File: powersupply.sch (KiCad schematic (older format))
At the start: 12 parts

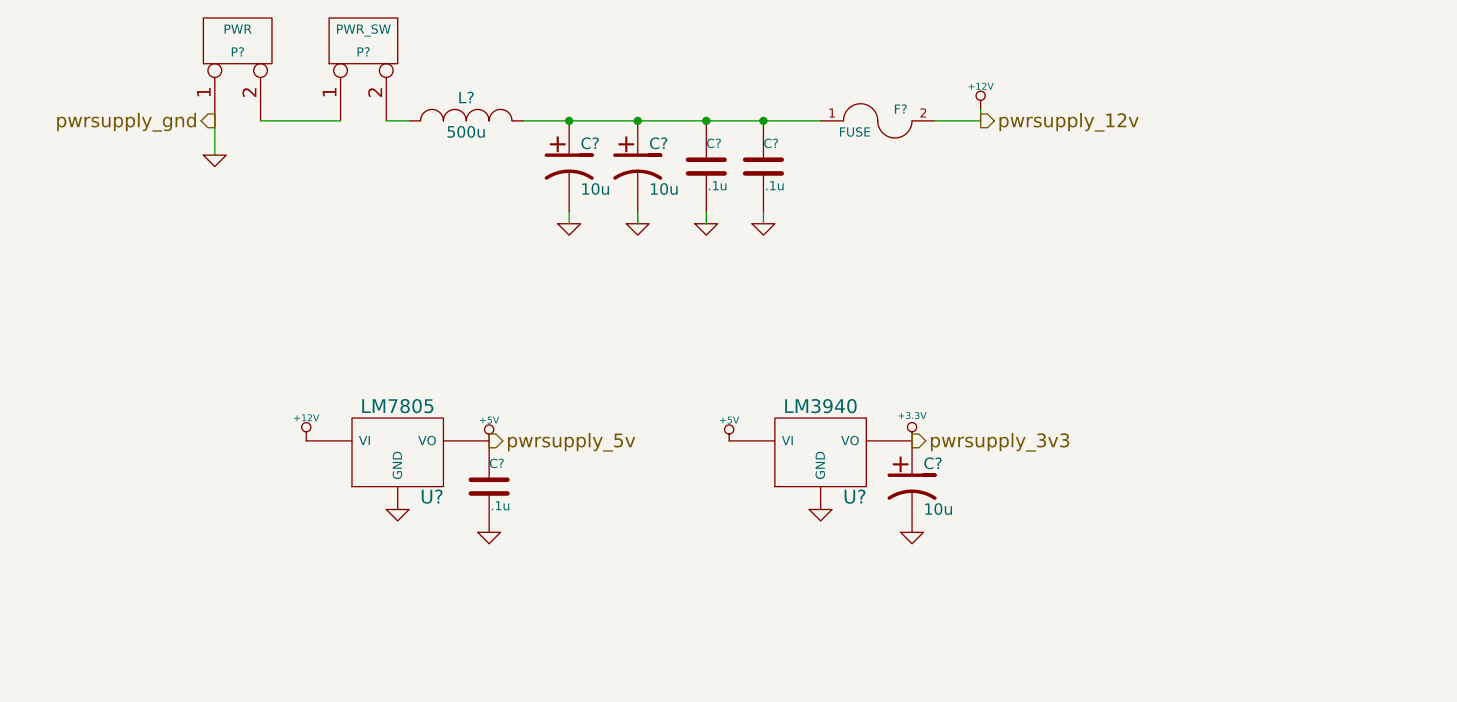
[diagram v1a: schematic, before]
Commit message: Annotated all schematics
- Added more caps to power supply
- Decided on power supply fuse part
- Changed 1n5711 SWR caps to BAT62
- Decided on MMBF170 for amp bias switch
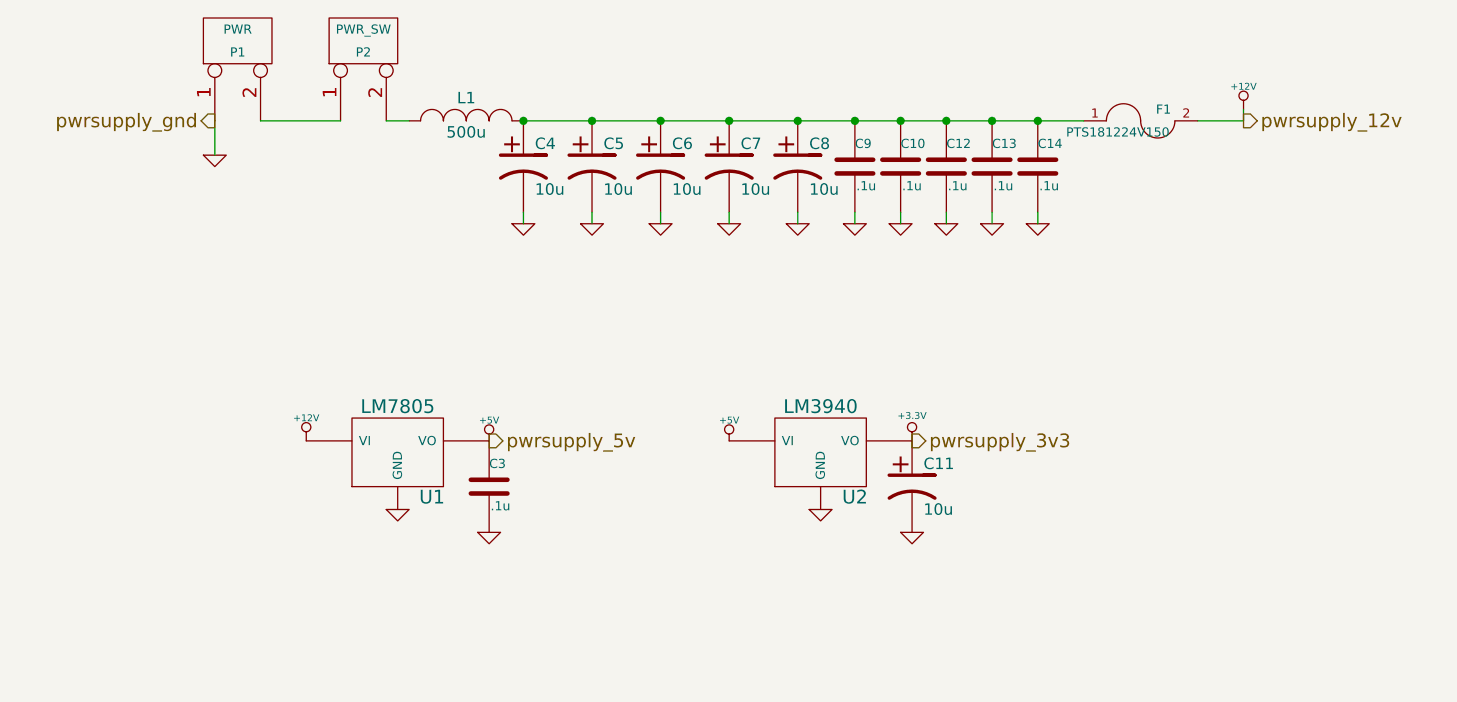
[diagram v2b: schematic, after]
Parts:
- removed C? (x2): .1u, symbol C
- added C10, C12, C13, C14, C9: .1u, symbol C
- added C6, C7, C8: 10u, symbol CP1
- F1: renamed from F?; value FUSE -> PTS181224V150
- gave numbers to parts that had none: 9
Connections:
- net GND: now also C10.2, C12.2, C13.2, C14.2, C6.2, C7.2, C8.2, C9.2
- net at C4.1, C5.1, F1.1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: now also C10.1, C12.1, C13.1, C14.1, C6.1, C7.1, C8.1, C9.1
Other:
- moved on the sheet: C4, C5, F1

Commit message: Associate more footprints
- Removed flyback diodes from amp
- Changed BAT62 -> SD101 (BAT62 is EOL)
- Changed R and C footprints for hand-soldered versions
- Associated through-hole cap footprints
- Associated regulator footprints
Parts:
- C10, C12, C13, C14, C3, C9: footprint (none) -> Capacitors_SMD:C_0805_HandSoldering
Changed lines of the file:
@@
 LIBS:transformers
 LIBS:qrpamp-cache
-EELAYER 24 0
+EELAYER 25 0
 EELAYER END
 $Descr A4 11693 8268
@@
 F 0 "P1" V 3150 2200 40  0000 C CNN
 F 1 "PWR" V 3250 2200 40  0000 C CNN
-F 2 "" H 3200 2200 60  0000 C CNN
+F 2 "" H 3200 2200 60  0001 C CNN
 F 3 "" H 3200 2200 60  0000 C CNN
 	1    3200 2200
@@
 F 0 "P2" V 3700 2200 40  0000 C CNN
 F 1 "PWR_SW" V 3800 2200 40  0000 C CNN
-F 2 "" H 3750 2200 60  0000 C CNN
+F 2 "" H 3750 2200 60  0001 C CNN
 F 3 "" H 3750 2200 60  0000 C CNN
 	1    3750 2200
@@
 F 0 "L1" H 4200 2650 50  0000 C CNN
 F 1 "500u" H 4200 2500 50  0000 C CNN
-F 2 "" H 4200 2550 60  0000 C CNN
+F 2 "" H 4200 2550 60  0001 C CNN
 F 3 "" H 4200 2550 60  0000 C CNN
 	1    4200 2550
@@
 F 0 "C4" H 4500 2850 50  0000 L CNN
 F 1 "10u" H 4500 2650 50  0000 L CNN
-F 2 "" H 4450 2750 60  0000 C CNN
+F 2 "" H 4450 2750 60  0001 C CNN
 F 3 "" H 4450 2750 60  0000 C CNN
 	1    4450 2750
@@
 F 0 "C5" H 4800 2850 50  0000 L CNN
 F 1 "10u" H 4800 2650 50  0000 L CNN
-F 2 "" H 4750 2750 60  0000 C CNN
+F 2 "" H 4750 2750 60  0001 C CNN
 F 3 "" H 4750 2750 60  0000 C CNN
 	1    4750 2750
@@
 F 0 "U1" H 4050 3804 60  0000 C CNN
 F 1 "LM7805" H 3900 4200 60  0000 C CNN
-F 2 "" H 3900 4000 60  0000 C CNN
+F 2 "" H 3900 4000 60  0001 C CNN
 F 3 "" H 3900 4000 60  0000 C CNN
 	1    3900 4000
@@
 F 0 "U2" H 5900 3804 60  0000 C CNN
 F 1 "LM3940" H 5750 4200 60  0000 C CNN
-F 2 "" H 5750 4000 60  0000 C CNN
+F 2 "" H 5750 4000 60  0001 C CNN
 F 3 "" H 5750 4000 60  0000 C CNN
 	1    5750 4000
@@
 F 0 "F1" H 7250 2600 40  0000 C CNN
 F 1 "PTS181224V150" H 7050 2500 40  0000 C CNN
-F 2 "" H 7150 2550 60  0000 C CNN
+F 2 "" H 7150 2550 60  0001 C CNN
 F 3 "" H 7150 2550 60  0000 C CNN
 	1    7150 2550
@@
 F 0 "C3" H 4300 4250 40  0000 L CNN
 F 1 ".1u" H 4306 4065 40  0000 L CNN
-F 2 "" H 4338 4000 30  0000 C CNN
+F 2 "Capacitors_SMD:C_0805_HandSoldering" H 4338 4000 30  0001 C CNN
 F 3 "" H 4300 4150 60  0000 C CNN
 	1    4300 4150
@@
 F 0 "C11" H 6200 4250 50  0000 L CNN
 F 1 "10u" H 6200 4050 50  0000 L CNN
-F 2 "" H 6150 4150 60  0000 C CNN
+F 2 "" H 6150 4150 60  0001 C CNN
 F 3 "" H 6150 4150 60  0000 C CNN
 	1    6150 4150
@@
 F 0 "C6" H 5100 2850 50  0000 L CNN
 F 1 "10u" H 5100 2650 50  0000 L CNN
-F 2 "" H 5050 2750 60  0000 C CNN
+F 2 "" H 5050 2750 60  0001 C CNN
 F 3 "" H 5050 2750 60  0000 C CNN
 	1    5050 2750
@@
 F 0 "C7" H 5400 2850 50  0000 L CNN
 F 1 "10u" H 5400 2650 50  0000 L CNN
-F 2 "" H 5350 2750 60  0000 C CNN
+F 2 "" H 5350 2750 60  0001 C CNN
 F 3 "" H 5350 2750 60  0000 C CNN
 	1    5350 2750
@@
 F 0 "C8" H 5700 2850 50  0000 L CNN
 F 1 "10u" H 5700 2650 50  0000 L CNN
-F 2 "" H 5650 2750 60  0000 C CNN
+F 2 "" H 5650 2750 60  0001 C CNN
 F 3 "" H 5650 2750 60  0000 C CNN
 	1    5650 2750
@@
 F 0 "C9" H 5900 2850 40  0000 L CNN
 F 1 ".1u" H 5906 2665 40  0000 L CNN
-F 2 "" H 5938 2600 30  0000 C CNN
+F 2 "Capacitors_SMD:C_0805_HandSoldering" H 5938 2600 30  0001 C CNN
 F 3 "" H 5900 2750 60  0000 C CNN
 	1    5900 2750
@@
 F 0 "C10" H 6100 2850 40  0000 L CNN
 F 1 ".1u" H 6106 2665 40  0000 L CNN
-F 2 "" H 6138 2600 30  0000 C CNN
+F 2 "Capacitors_SMD:C_0805_HandSoldering" H 6138 2600 30  0001 C CNN
 F 3 "" H 6100 2750 60  0000 C CNN
 	1    6100 2750
@@
 F 0 "C12" H 6300 2850 40  0000 L CNN
 F 1 ".1u" H 6306 2665 40  0000 L CNN
-F 2 "" H 6338 2600 30  0000 C CNN
+F 2 "Capacitors_SMD:C_0805_HandSoldering" H 6338 2600 30  0001 C CNN
 F 3 "" H 6300 2750 60  0000 C CNN
 	1    6300 2750
@@
 F 0 "C13" H 6500 2850 40  0000 L CNN
 F 1 ".1u" H 6506 2665 40  0000 L CNN
-F 2 "" H 6538 2600 30  0000 C CNN
+F 2 "Capacitors_SMD:C_0805_HandSoldering" H 6538 2600 30  0001 C CNN
 F 3 "" H 6500 2750 60  0000 C CNN
 	1    6500 2750
@@
 F 0 "C14" H 6700 2850 40  0000 L CNN
 F 1 ".1u" H 6706 2665 40  0000 L CNN
-F 2 "" H 6738 2600 30  0000 C CNN
+F 2 "Capacitors_SMD:C_0805_HandSoldering" H 6738 2600 30  0001 C CNN
 F 3 "" H 6700 2750 60  0000 C CNN
 	1    6700 2750

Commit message: Finished band filters schematic
- Associated last of the capacitors with footprints
- Associated inductors
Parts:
- C11, C4, C5, C6, C7, C8: footprint (none) -> Capacitors_ThroughHole:Capacitor5x11RM2.5
- U1: footprint (none) -> SMD_Packages:DPAK-2
- U2: footprint (none) -> SMD_Packages:TO-263
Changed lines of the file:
@@
 	3300 2550 3650 2550
 $Comp
-L GND #PWR20
+L GND #PWR020
 U 1 1 5470C747
 P 3100 2700
-F 0 "#PWR20" H 3100 2700 30  0001 C CNN
+F 0 "#PWR020" H 3100 2700 30  0001 C CNN
 F 1 "GND" H 3100 2630 30  0001 C CNN
 F 2 "" H 3100 2700 60  0000 C CNN
@@
 F 0 "C4" H 4500 2850 50  0000 L CNN
 F 1 "10u" H 4500 2650 50  0000 L CNN
-F 2 "" H 4450 2750 60  0001 C CNN
+F 2 "Capacitors_ThroughHole:Capacitor5x11RM2.5" H 4450 2750 60  0001 C CNN
 F 3 "" H 4450 2750 60  0000 C CNN
 	1    4450 2750
@@
 F 0 "C5" H 4800 2850 50  0000 L CNN
 F 1 "10u" H 4800 2650 50  0000 L CNN
-F 2 "" H 4750 2750 60  0001 C CNN
+F 2 "Capacitors_ThroughHole:Capacitor5x11RM2.5" H 4750 2750 60  0001 C CNN
 F 3 "" H 4750 2750 60  0000 C CNN
 	1    4750 2750
@@
 $EndComp
 $Comp
-L GND #PWR25
+L GND #PWR021
 U 1 1 5470C830
 P 4450 3000
-F 0 "#PWR25" H 4450 3000 30  0001 C CNN
+F 0 "#PWR021" H 4450 3000 30  0001 C CNN
 F 1 "GND" H 4450 2930 30  0001 C CNN
 F 2 "" H 4450 3000 60  0000 C CNN
@@
 $EndComp
 $Comp
-L GND #PWR26
+L GND #PWR022
 U 1 1 5470C83B
 P 4750 3000
-F 0 "#PWR26" H 4750 3000 30  0001 C CNN
+F 0 "#PWR022" H 4750 3000 30  0001 C CNN
 F 1 "GND" H 4750 2930 30  0001 C CNN
 F 2 "" H 4750 3000 60  0000 C CNN
@@
 	4750 2950 4750 3000
 $Comp
-L +12V #PWR39
+L +12V #PWR023
 U 1 1 5470C933
 P 7600 2500
-F 0 "#PWR39" H 7600 2450 20  0001 C CNN
+F 0 "#PWR023" H 7600 2450 20  0001 C CNN
 F 1 "+12V" H 7600 2600 30  0000 C CNN
 F 2 "" H 7600 2500 60  0000 C CNN
@@
 F 0 "U1" H 4050 3804 60  0000 C CNN
 F 1 "LM7805" H 3900 4200 60  0000 C CNN
-F 2 "" H 3900 4000 60  0001 C CNN
+F 2 "SMD_Packages:DPAK-2" H 3900 4000 60  0001 C CNN
 F 3 "" H 3900 4000 60  0000 C CNN
 	1    3900 4000
@@
 F 0 "U2" H 5900 3804 60  0000 C CNN
 F 1 "LM3940" H 5750 4200 60  0000 C CNN
-F 2 "" H 5750 4000 60  0001 C CNN
+F 2 "SMD_Packages:TO-263" H 5750 4000 60  0001 C CNN
 F 3 "" H 5750 4000 60  0000 C CNN
 	1    5750 4000
@@
 	7600 2550 7600 2500
 $Comp
-L GND #PWR22
+L GND #PWR024
 U 1 1 5470CBF4
 P 3900 4250
-F 0 "#PWR22" H 3900 4250 30  0001 C CNN
+F 0 "#PWR024" H 3900 4250 30  0001 C CNN
 F 1 "GND" H 3900 4180 30  0001 C CNN
 F 2 "" H 3900 4250 60  0000 C CNN
@@
 $EndComp
 $Comp
-L GND #PWR31
+L GND #PWR025
 U 1 1 5470CBFF
 P 5750 4250
-F 0 "#PWR31" H 5750 4250 30  0001 C CNN
+F 0 "#PWR025" H 5750 4250 30  0001 C CNN
 F 1 "GND" H 5750 4180 30  0001 C CNN
 F 2 "" H 5750 4250 60  0000 C CNN
@@
 $EndComp
 $Comp
-L +12V #PWR21
+L +12V #PWR026
 U 1 1 5470CC17
 P 3500 3950
-F 0 "#PWR21" H 3500 3900 20  0001 C CNN
+F 0 "#PWR026" H 3500 3900 20  0001 C CNN
 F 1 "+12V" H 3500 4050 30  0000 C CNN
 F 2 "" H 3500 3950 60  0000 C CNN
@@
 $EndComp
 $Comp
-L +5V #PWR23
+L +5V #PWR027
 U 1 1 5470CC25
 P 4300 3950
-F 0 "#PWR23" H 4300 4040 20  0001 C CNN
+F 0 "#PWR027" H 4300 4040 20  0001 C CNN
 F 1 "+5V" H 4300 4040 30  0000 C CNN
 F 2 "" H 4300 3950 60  0000 C CNN
@@
 $EndComp
 $Comp
-L +5V #PWR29
+L +5V #PWR028
 U 1 1 5470CC37
 P 5350 3950
-F 0 "#PWR29" H 5350 4040 20  0001 C CNN
+F 0 "#PWR028" H 5350 4040 20  0001 C CNN
 F 1 "+5V" H 5350 4040 30  0000 C CNN
 F 2 "" H 5350 3950 60  0000 C CNN
@@
 $EndComp
 $Comp
-L +3.3V #PWR34
+L +3.3V #PWR029
 U 1 1 5470CC44
 P 6150 3950
-F 0 "#PWR34" H 6150 3910 30  0001 C CNN
+F 0 "#PWR029" H 6150 3910 30  0001 C CNN
 F 1 "+3.3V" H 6150 4060 30  0000 C CNN
 F 2 "" H 6150 3950 60  0000 C CNN
@@
 F 0 "C11" H 6200 4250 50  0000 L CNN
 F 1 "10u" H 6200 4050 50  0000 L CNN
-F 2 "" H 6150 4150 60  0001 C CNN
+F 2 "Capacitors_ThroughHole:Capacitor5x11RM2.5" H 6150 4150 60  0001 C CNN
 F 3 "" H 6150 4150 60  0000 C CNN
 	1    6150 4150
@@
 $EndComp
 $Comp
-L GND #PWR24
+L GND #PWR030
 U 1 1 5470CCF4
 P 4300 4350
-F 0 "#PWR24" H 4300 4350 30  0001 C CNN
+F 0 "#PWR030" H 4300 4350 30  0001 C CNN
 F 1 "GND" H 4300 4280 30  0001 C CNN
 F 2 "" H 4300 4350 60  0000 C CNN
@@
 $EndComp
 $Comp
-L GND #PWR35
+L GND #PWR031
 U 1 1 5470CCFF
 P 6150 4350
-F 0 "#PWR35" H 6150 4350 30  0001 C CNN
+F 0 "#PWR031" H 6150 4350 30  0001 C CNN
 F 1 "GND" H 6150 4280 30  0001 C CNN
 F 2 "" H 6150 4350 60  0000 C CNN
@@
 F 0 "C6" H 5100 2850 50  0000 L CNN
 F 1 "10u" H 5100 2650 50  0000 L CNN
-F 2 "" H 5050 2750 60  0001 C CNN
+F 2 "Capacitors_ThroughHole:Capacitor5x11RM2.5" H 5050 2750 60  0001 C CNN
 F 3 "" H 5050 2750 60  0000 C CNN
 	1    5050 2750
@@
 F 0 "C7" H 5400 2850 50  0000 L CNN
 F 1 "10u" H 5400 2650 50  0000 L CNN
-F 2 "" H 5350 2750 60  0001 C CNN
+F 2 "Capacitors_ThroughHole:Capacitor5x11RM2.5" H 5350 2750 60  0001 C CNN
 F 3 "" H 5350 2750 60  0000 C CNN
 	1    5350 2750
@@
 F 0 "C8" H 5700 2850 50  0000 L CNN
 F 1 "10u" H 5700 2650 50  0000 L CNN
-F 2 "" H 5650 2750 60  0001 C CNN
+F 2 "Capacitors_ThroughHole:Capacitor5x11RM2.5" H 5650 2750 60  0001 C CNN
 F 3 "" H 5650 2750 60  0000 C CNN
 	1    5650 2750
@@
 $EndComp
 $Comp
-L GND #PWR27
+L GND #PWR032
 U 1 1 54789812
 P 5050 3000
-F 0 "#PWR27" H 5050 3000 30  0001 C CNN
+F 0 "#PWR032" H 5050 3000 30  0001 C CNN
 F 1 "GND" H 5050 2930 30  0001 C CNN
 F 2 "" H 5050 3000 60  0000 C CNN
@@
 $EndComp
 $Comp
-L GND #PWR28
+L GND #PWR033
 U 1 1 5478981D
 P 5350 3000
-F 0 "#PWR28" H 5350 3000 30  0001 C CNN
+F 0 "#PWR033" H 5350 3000 30  0001 C CNN
 F 1 "GND" H 5350 2930 30  0001 C CNN
 F 2 "" H 5350 3000 60  0000 C CNN
@@
 $EndComp
 $Comp
-L GND #PWR30
+L GND #PWR034
 U 1 1 54789828
 P 5650 3000
-F 0 "#PWR30" H 5650 3000 30  0001 C CNN
+F 0 "#PWR034" H 5650 3000 30  0001 C CNN
 F 1 "GND" H 5650 2930 30  0001 C CNN
 F 2 "" H 5650 3000 60  0000 C CNN
@@
 $EndComp
 $Comp
-L GND #PWR32
+L GND #PWR035
 U 1 1 54789833
 P 5900 3000
-F 0 "#PWR32" H 5900 3000 30  0001 C CNN
+F 0 "#PWR035" H 5900 3000 30  0001 C CNN
 F 1 "GND" H 5900 2930 30  0001 C CNN
 F 2 "" H 5900 3000 60  0000 C CNN
@@
 $EndComp
 $Comp
-L GND #PWR33
+L GND #PWR036
 U 1 1 5478983E
 P 6100 3000
-F 0 "#PWR33" H 6100 3000 30  0001 C CNN
+F 0 "#PWR036" H 6100 3000 30  0001 C CNN
 F 1 "GND" H 6100 2930 30  0001 C CNN
 F 2 "" H 6100 3000 60  0000 C CNN
@@
 $EndComp
 $Comp
-L GND #PWR36
+L GND #PWR037
 U 1 1 54789849
 P 6300 3000
-F 0 "#PWR36" H 6300 3000 30  0001 C CNN
+F 0 "#PWR037" H 6300 3000 30  0001 C CNN
 F 1 "GND" H 6300 2930 30  0001 C CNN
 F 2 "" H 6300 3000 60  0000 C CNN
@@
 $EndComp
 $Comp
-L GND #PWR37
+L GND #PWR038
 U 1 1 54789854
 P 6500 3000
-F 0 "#PWR37" H 6500 3000 30  0001 C CNN
+F 0 "#PWR038" H 6500 3000 30  0001 C CNN
 F 1 "GND" H 6500 2930 30  0001 C CNN
 F 2 "" H 6500 3000 60  0000 C CNN
@@
 $EndComp
 $Comp
-L GND #PWR38
+L GND #PWR039
 U 1 1 5478985F
 P 6700 3000
-F 0 "#PWR38" H 6700 3000 30  0001 C CNN
+F 0 "#PWR039" H 6700 3000 30  0001 C CNN
 F 1 "GND" H 6700 2930 30  0001 C CNN
 F 2 "" H 6700 3000 60  0000 C CNN

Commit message: Finished associating relays
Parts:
- L1: footprint (none) -> nu9j-footprints:TOROID-50
- P1: footprint (none) -> nu9j-footprints:PWR2-16AWG
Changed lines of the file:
@@
 LIBS:mcus
 LIBS:transformers
+LIBS:relays
 LIBS:qrpamp-cache
 EELAYER 25 0
@@
 F 0 "P1" V 3150 2200 40  0000 C CNN
 F 1 "PWR" V 3250 2200 40  0000 C CNN
-F 2 "" H 3200 2200 60  0001 C CNN
+F 2 "nu9j-footprints:PWR2-16AWG" H 3200 2200 60  0001 C CNN
 F 3 "" H 3200 2200 60  0000 C CNN
 	1    3200 2200
@@
 	3300 2550 3650 2550
 $Comp
-L GND #PWR020
+L GND #PWR20
 U 1 1 5470C747
 P 3100 2700
-F 0 "#PWR020" H 3100 2700 30  0001 C CNN
+F 0 "#PWR20" H 3100 2700 30  0001 C CNN
 F 1 "GND" H 3100 2630 30  0001 C CNN
 F 2 "" H 3100 2700 60  0000 C CNN
@@
 F 0 "L1" H 4200 2650 50  0000 C CNN
 F 1 "500u" H 4200 2500 50  0000 C CNN
-F 2 "" H 4200 2550 60  0001 C CNN
+F 2 "nu9j-footprints:TOROID-50" H 4200 2550 60  0001 C CNN
 F 3 "" H 4200 2550 60  0000 C CNN
 	1    4200 2550
@@
 $EndComp
 $Comp
-L GND #PWR021
+L GND #PWR25
 U 1 1 5470C830
 P 4450 3000
-F 0 "#PWR021" H 4450 3000 30  0001 C CNN
+F 0 "#PWR25" H 4450 3000 30  0001 C CNN
 F 1 "GND" H 4450 2930 30  0001 C CNN
 F 2 "" H 4450 3000 60  0000 C CNN
@@
 $EndComp
 $Comp
-L GND #PWR022
+L GND #PWR26
 U 1 1 5470C83B
 P 4750 3000
-F 0 "#PWR022" H 4750 3000 30  0001 C CNN
+F 0 "#PWR26" H 4750 3000 30  0001 C CNN
 F 1 "GND" H 4750 2930 30  0001 C CNN
 F 2 "" H 4750 3000 60  0000 C CNN
@@
 	4750 2950 4750 3000
 $Comp
-L +12V #PWR023
+L +12V #PWR39
 U 1 1 5470C933
 P 7600 2500
-F 0 "#PWR023" H 7600 2450 20  0001 C CNN
+F 0 "#PWR39" H 7600 2450 20  0001 C CNN
 F 1 "+12V" H 7600 2600 30  0000 C CNN
 F 2 "" H 7600 2500 60  0000 C CNN
@@
 	7600 2550 7600 2500
 $Comp
-L GND #PWR024
+L GND #PWR22
 U 1 1 5470CBF4
 P 3900 4250
-F 0 "#PWR024" H 3900 4250 30  0001 C CNN
+F 0 "#PWR22" H 3900 4250 30  0001 C CNN
 F 1 "GND" H 3900 4180 30  0001 C CNN
 F 2 "" H 3900 4250 60  0000 C CNN
@@
 $EndComp
 $Comp
-L GND #PWR025
+L GND #PWR31
 U 1 1 5470CBFF
 P 5750 4250
-F 0 "#PWR025" H 5750 4250 30  0001 C CNN
+F 0 "#PWR31" H 5750 4250 30  0001 C CNN
 F 1 "GND" H 5750 4180 30  0001 C CNN
 F 2 "" H 5750 4250 60  0000 C CNN
@@
 $EndComp
 $Comp
-L +12V #PWR026
+L +12V #PWR21
 U 1 1 5470CC17
 P 3500 3950
-F 0 "#PWR026" H 3500 3900 20  0001 C CNN
+F 0 "#PWR21" H 3500 3900 20  0001 C CNN
 F 1 "+12V" H 3500 4050 30  0000 C CNN
 F 2 "" H 3500 3950 60  0000 C CNN
@@
 $EndComp
 $Comp
-L +5V #PWR027
+L +5V #PWR23
 U 1 1 5470CC25
 P 4300 3950
-F 0 "#PWR027" H 4300 4040 20  0001 C CNN
+F 0 "#PWR23" H 4300 4040 20  0001 C CNN
 F 1 "+5V" H 4300 4040 30  0000 C CNN
 F 2 "" H 4300 3950 60  0000 C CNN
@@
 $EndComp
 $Comp
-L +5V #PWR028
+L +5V #PWR29
 U 1 1 5470CC37
 P 5350 3950
-F 0 "#PWR028" H 5350 4040 20  0001 C CNN
+F 0 "#PWR29" H 5350 4040 20  0001 C CNN
 F 1 "+5V" H 5350 4040 30  0000 C CNN
 F 2 "" H 5350 3950 60  0000 C CNN
@@
 $EndComp
 $Comp
-L +3.3V #PWR029
+L +3.3V #PWR34
 U 1 1 5470CC44
 P 6150 3950
-F 0 "#PWR029" H 6150 3910 30  0001 C CNN
+F 0 "#PWR34" H 6150 3910 30  0001 C CNN
 F 1 "+3.3V" H 6150 4060 30  0000 C CNN
 F 2 "" H 6150 3950 60  0000 C CNN
@@
 $EndComp
 $Comp
-L GND #PWR030
+L GND #PWR24
 U 1 1 5470CCF4
 P 4300 4350
-F 0 "#PWR030" H 4300 4350 30  0001 C CNN
+F 0 "#PWR24" H 4300 4350 30  0001 C CNN
 F 1 "GND" H 4300 4280 30  0001 C CNN
 F 2 "" H 4300 4350 60  0000 C CNN
@@
 $EndComp
 $Comp
-L GND #PWR031
+L GND #PWR35
 U 1 1 5470CCFF
 P 6150 4350
-F 0 "#PWR031" H 6150 4350 30  0001 C CNN
+F 0 "#PWR35" H 6150 4350 30  0001 C CNN
 F 1 "GND" H 6150 4280 30  0001 C CNN
 F 2 "" H 6150 4350 60  0000 C CNN
@@
 $EndComp
 $Comp
-L GND #PWR032
+L GND #PWR27
 U 1 1 54789812
 P 5050 3000
-F 0 "#PWR032" H 5050 3000 30  0001 C CNN
+F 0 "#PWR27" H 5050 3000 30  0001 C CNN
 F 1 "GND" H 5050 2930 30  0001 C CNN
 F 2 "" H 5050 3000 60  0000 C CNN
@@
 $EndComp
 $Comp
-L GND #PWR033
+L GND #PWR28
 U 1 1 5478981D
 P 5350 3000
-F 0 "#PWR033" H 5350 3000 30  0001 C CNN
+F 0 "#PWR28" H 5350 3000 30  0001 C CNN
 F 1 "GND" H 5350 2930 30  0001 C CNN
 F 2 "" H 5350 3000 60  0000 C CNN
@@
 $EndComp
 $Comp
-L GND #PWR034
+L GND #PWR30
 U 1 1 54789828
 P 5650 3000
-F 0 "#PWR034" H 5650 3000 30  0001 C CNN
+F 0 "#PWR30" H 5650 3000 30  0001 C CNN
 F 1 "GND" H 5650 2930 30  0001 C CNN
 F 2 "" H 5650 3000 60  0000 C CNN
@@
 $EndComp
 $Comp
-L GND #PWR035
+L GND #PWR32
 U 1 1 54789833
 P 5900 3000
-F 0 "#PWR035" H 5900 3000 30  0001 C CNN
+F 0 "#PWR32" H 5900 3000 30  0001 C CNN
 F 1 "GND" H 5900 2930 30  0001 C CNN
 F 2 "" H 5900 3000 60  0000 C CNN
@@
 $EndComp
 $Comp
-L GND #PWR036
+L GND #PWR33
 U 1 1 5478983E
 P 6100 3000
-F 0 "#PWR036" H 6100 3000 30  0001 C CNN
+F 0 "#PWR33" H 6100 3000 30  0001 C CNN
 F 1 "GND" H 6100 2930 30  0001 C CNN
 F 2 "" H 6100 3000 60  0000 C CNN
@@
 $EndComp
 $Comp
-L GND #PWR037
+L GND #PWR36
 U 1 1 54789849
 P 6300 3000
-F 0 "#PWR037" H 6300 3000 30  0001 C CNN
+F 0 "#PWR36" H 6300 3000 30  0001 C CNN
 F 1 "GND" H 6300 2930 30  0001 C CNN
 F 2 "" H 6300 3000 60  0000 C CNN
@@
 $EndComp
 $Comp
-L GND #PWR038
+L GND #PWR37
 U 1 1 54789854
 P 6500 3000
-F 0 "#PWR038" H 6500 3000 30  0001 C CNN
+F 0 "#PWR37" H 6500 3000 30  0001 C CNN
 F 1 "GND" H 6500 2930 30  0001 C CNN
 F 2 "" H 6500 3000 60  0000 C CNN
@@
 $EndComp
 $Comp
-L GND #PWR039
+L GND #PWR38
 U 1 1 5478985F
 P 6700 3000
-F 0 "#PWR039" H 6700 3000 30  0001 C CNN
+F 0 "#PWR38" H 6700 3000 30  0001 C CNN
 F 1 "GND" H 6700 2930 30  0001 C CNN
 F 2 "" H 6700 3000 60  0000 C CNN
